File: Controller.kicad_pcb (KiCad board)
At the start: 2 copper layers, 52.1 x 85.1 mm, 18 parts, among them IC1 SN74HCT245PWR, J1 RGB_3_pin, J2 RGB_3_pin, J3 RGB_3_pin, J4 RGB_3_pin, J5 RGB_3_pin, J6 RGB_3_pin, J7 RGB_3_pin, J8 RGB_3_pin, J9 AMP_Mate-N-Lok_Power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

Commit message: Add top and bottom plate files.
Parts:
- renumbered REF** to H5, REF** to H6

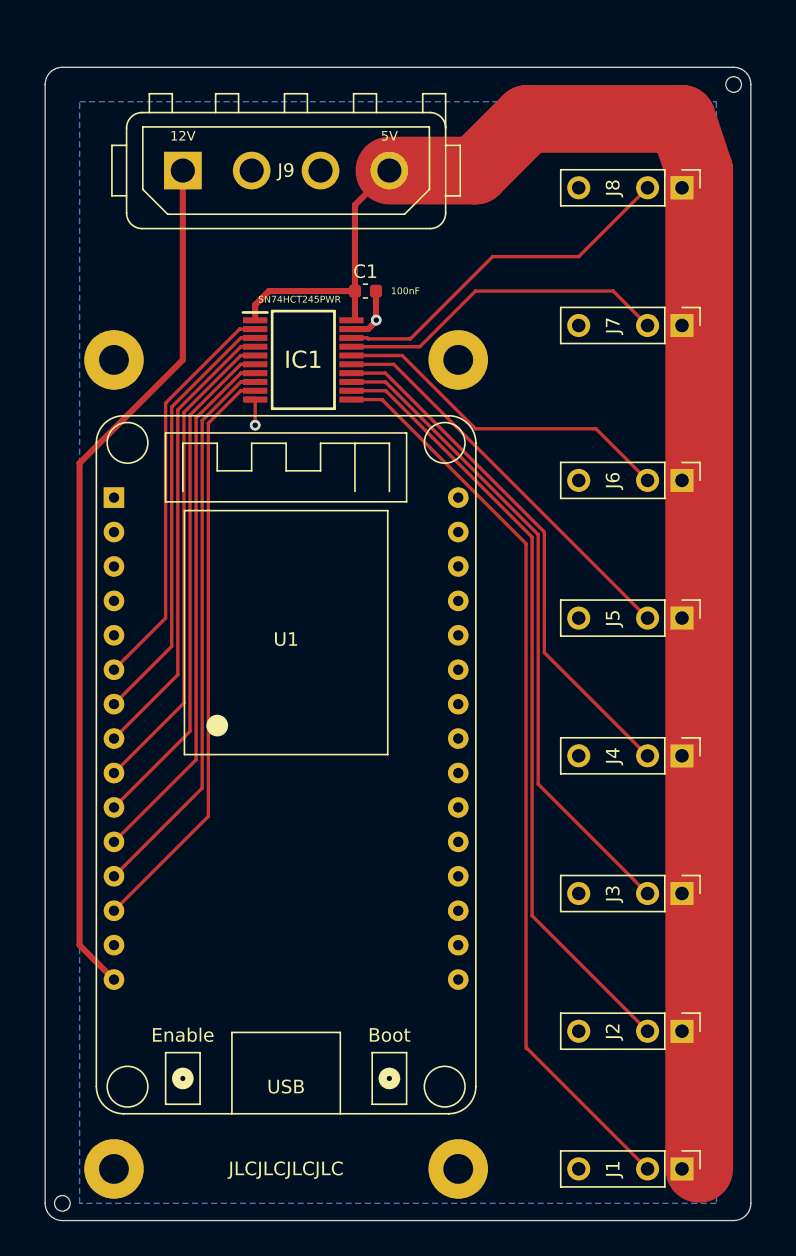
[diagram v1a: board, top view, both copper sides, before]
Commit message: More compact layout with 10 channels.
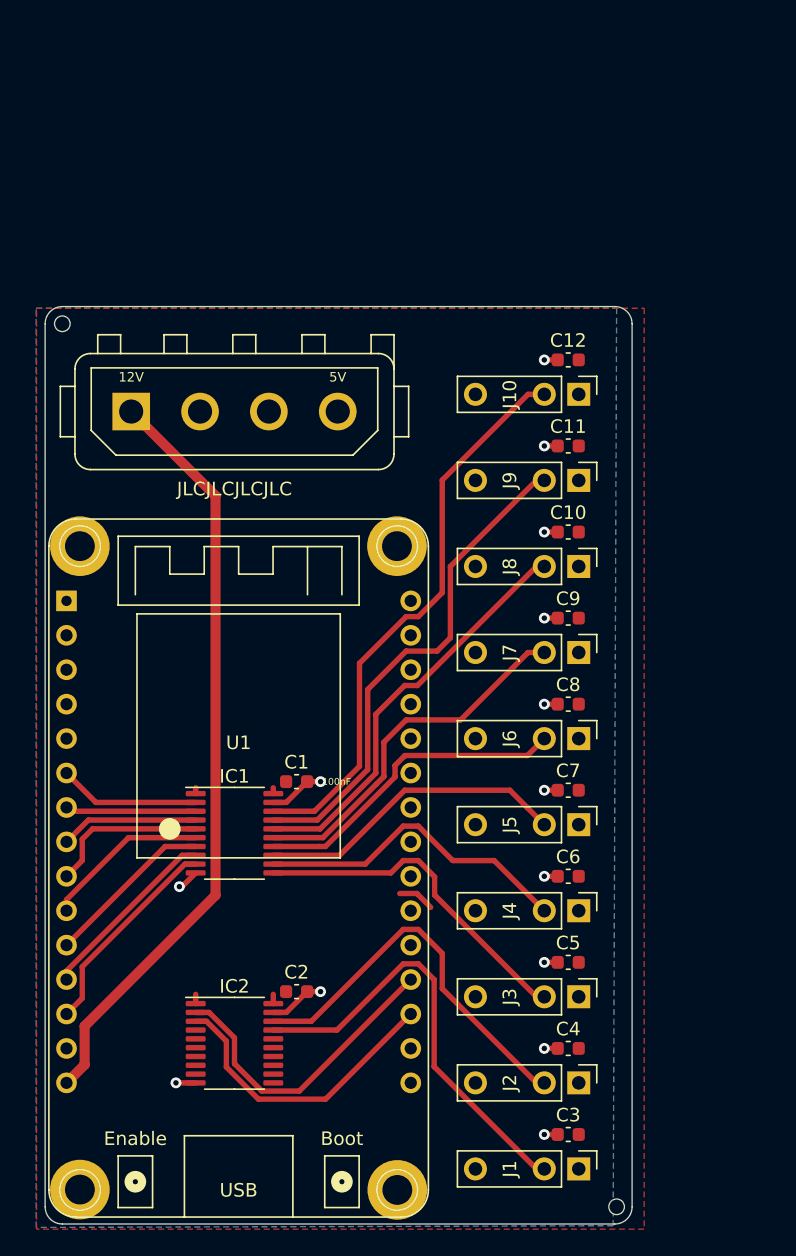
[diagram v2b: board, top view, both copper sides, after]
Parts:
- added C10: 1000nF, Capacitor_SMD:C_0603_1608Metric, F.Cu at (182.1, 95.2)
- added C11: 1000nF, Capacitor_SMD:C_0603_1608Metric, F.Cu at (182.1, 88.9)
- added C12: 1000nF, Capacitor_SMD:C_0603_1608Metric, F.Cu at (182.1, 82.5)
- added C2: 100nF, Capacitor_SMD:C_0603_1608Metric, F.Cu at (162.1, 129.2)
- added C3: 1000nF, Capacitor_SMD:C_0603_1608Metric, F.Cu at (182.1, 139.7)
- added C4: 1000nF, Capacitor_SMD:C_0603_1608Metric, F.Cu at (182.1, 133.3)
- added C5: 1000nF, Capacitor_SMD:C_0603_1608Metric, F.Cu at (182.1, 127.0)
- added C6: 1000nF, Capacitor_SMD:C_0603_1608Metric, F.Cu at (182.1, 120.7)
- added C7: 1000nF, Capacitor_SMD:C_0603_1608Metric, F.Cu at (182.1, 114.3)
- added C8: 1000nF, Capacitor_SMD:C_0603_1608Metric, F.Cu at (182.1, 108.0)
- added C9: 1000nF, Capacitor_SMD:C_0603_1608Metric, F.Cu at (182.1, 101.6)
- added IC2: SN74HCT245PWR, Package_SO:TSSOP-20_4.4x6.5mm_P0.65mm, F.Cu at (157.5, 133.0)
- added J10: RGB_3_pin, local:RGB_3-Pin, F.Cu at (182.9, 85.1)
- added Je: AMP_Mate-N-Lok_Power, local:TE_MATE-N-LOK_350211-1_1x04_P5.08mm_Vertical, F.Cu at (149.9, 86.4)
- IC1: footprint local:SN74HCT245DBR -> Package_SO:TSSOP-20_4.4x6.5mm_P0.65mm
- J9: value AMP_Mate-N-Lok_Power -> RGB_3_pin; footprint local:TE_MATE-N-LOK_350211-1_1x04_P5.08mm_Vertical -> local:RGB_3-Pin
- moved H6 52.6 mm to (144.8, 79.9)
- moved H5 40.9 mm to (185.7, 145.0)
- moved J9 37.1 mm to (182.9, 91.4), turned to 270 degrees
- moved C1 36.5 mm to (162.1, 113.7)
- moved IC1 35.3 mm to (157.5, 117.5)
- moved J8 29.0 mm to (182.9, 97.8)
- moved J7 25.3 mm to (182.9, 104.1)
- moved J6 20.5 mm to (182.9, 110.5)
- moved J5 17.0 mm to (182.9, 116.8)
- moved H2 14.5 mm to (169.5, 96.3)
- moved H1 14.0 mm to (146.1, 96.3)
- moved J4 13.7 mm to (182.9, 123.2)
- moved J3 10.8 mm to (182.9, 129.5)
- moved J2 8.52 mm to (182.9, 135.9)
- moved U1 8.39 mm to (157.8, 100.3)
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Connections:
- J1 pad 2: /B8 -> /B10
- J2 pad 2: /B7 -> /B9
- J3 pad 2: /B6 -> /B8
- J4 pad 2: /B5 -> /B7
- J5 pad 2: /B4 -> /B6
- J6 pad 2: /B3 -> /B5
- J7 pad 2: /B2 -> /B4
- J8 pad 2: /B1 -> /B3
- J9 pad 1: +12V -> +5V
- J9 pad 2: GND -> /B2
- U1 pad 18: Net-(U1-Pad18) -> /A10
- U1 pad 19: Net-(U1-Pad19) -> /A9
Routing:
- net +5V: track 124.1 -> 2.25 mm
- net /B8: track 67.2 -> 25.3 mm
- net /B7: track 57.8 -> 23.7 mm
- net /B10: track 0.00 -> 32.0 mm
- net /B9: track 0.00 -> 29.0 mm
- net /A8: track 43.3 -> 15.5 mm
- net /A7: track 41.4 -> 13.7 mm
- net /A6: track 39.5 -> 12.5 mm
- net /A5: track 37.6 -> 12.2 mm
- net /B6: track 48.3 -> 23.0 mm
- net /A3: track 34.5 -> 10.2 mm
- net /A4: track 35.7 -> 11.9 mm
- net /A9: track 0.00 -> 22.8 mm
- net /A2: track 32.0 -> 9.65 mm
- net /A10: track 0.00 -> 22.0 mm
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- added copper zone on F.Cu, net +5V
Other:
- board size 52.1 x 85.1 mm -> 43.3 x 67.7 mm

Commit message: Update controller to new design.
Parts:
- removed C10, C11, C12, C5, C6, C7, C8, C9: 1000nF, Capacitor_SMD:C_0603_1608Metric
- C3: value 1000nF -> 100nF
- C4: value 1000nF -> 47uF
- H5, H6: value ToolingHole_1.152mm -> MountingHole
- moved H6 77.3 mm to (185.9, 145.3)
- moved H5 77.2 mm to (144.5, 79.8)
- moved C3 34.7 mm to (147.6, 136.7), turned to 180 degrees
- moved C4 34.6 mm to (147.6, 135.1)
- renumbered Je to J11
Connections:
- C4 pad 1: GND -> +5V
- C4 pad 2: +5V -> GND
- IC2 pad 11: Net-(IC2-Pad11) -> (no net)
- IC2 pad 12: Net-(IC2-Pad12) -> (no net)
- IC2 pad 13: Net-(IC2-Pad13) -> (no net)
- IC2 pad 14: Net-(IC2-Pad14) -> (no net)
- IC2 pad 15: Net-(IC2-Pad15) -> (no net)
- IC2 pad 16: Net-(IC2-Pad16) -> (no net)
- IC2 pad 4: Net-(IC2-Pad4) -> (no net)
- IC2 pad 5: Net-(IC2-Pad5) -> (no net)
- IC2 pad 6: Net-(IC2-Pad6) -> (no net)
- IC2 pad 7: Net-(IC2-Pad7) -> (no net)
- IC2 pad 8: Net-(IC2-Pad8) -> (no net)
- IC2 pad 9: Net-(IC2-Pad9) -> (no net)
- J11 pad 1: +12V -> (no net)
- U1 pad 1: Net-(U1-Pad1) -> (no net)
- U1 pad 15: +12V -> +5V
- U1 pad 16: Net-(U1-Pad16) -> (no net)
- U1 pad 2: Net-(U1-Pad2) -> (no net)
- U1 pad 20: Net-(U1-Pad20) -> (no net)
- U1 pad 21: Net-(U1-Pad21) -> (no net)
- U1 pad 22: Net-(U1-Pad22) -> (no net)
- U1 pad 23: Net-(U1-Pad23) -> (no net)
- U1 pad 24: Net-(U1-Pad24) -> (no net)
- U1 pad 25: Net-(U1-Pad25) -> (no net)
- U1 pad 26: Net-(U1-Pad26) -> (no net)
- U1 pad 27: Net-(U1-Pad27) -> (no net)
- U1 pad 28: Net-(U1-Pad28) -> (no net)
- U1 pad 29: Net-(U1-Pad29) -> (no net)
- U1 pad 3: Net-(U1-Pad3) -> (no net)
- U1 pad 30: Net-(U1-Pad30) -> (no net)
- U1 pad 4: Net-(U1-Pad4) -> (no net)
- U1 pad 5: Net-(U1-Pad5) -> (no net)
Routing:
- net +12V: track 56.7 -> 0.00 mm
- net GND: track 21.2 -> 17.1 mm, vias 14 -> 4
- net +5V: track 2.25 -> 4.96 mm
- net (no net): track 2.71 -> 0.00 mm
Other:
- board size 43.3 x 67.7 mm -> 43.3 x 67.5 mm
